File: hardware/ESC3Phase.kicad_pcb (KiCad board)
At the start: 2 copper layers, 0 parts

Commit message: PCB layout: board outline, mounting holes, footprint placement, copper pours, phase-output routing
- 100x115mm 2-layer board, 4x M3 mounting holes, design rules per PowerLab spec
- All 55 schematic components synced to board with real footprints
- Auto-placed via force-directed placement with locked connector/MCU anchors
- GND pour (both layers) + localized pours for VIN_RAW/+VBUS/+VBUS_EFUSE_OUT/+VBUS_PROT/+5V_LOGIC
- Routed the 3 critical phase-output traces (SHA/SHB/SHC, 2mm wide)
- Documented full PCB status in ARCHITECTURE.md: NOT yet fab-ready (732 DRC
  violations, 21 courtyard overlaps, ~50 signal nets still unrouted since
  Freerouting is unavailable in this environment)

Co-Authored-By: Claude Sonnet 5 <noreply@anthropic.com>
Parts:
- added C1: 100 nF, METUPowerLab_Capacitors_Ceramics_SurfaceMounts:0603_Medium, F.Cu at (70.1, 21.5)
- added C10: 100 nF, METUPowerLab_Capacitors_Ceramics_SurfaceMounts:0603_Medium, F.Cu at (46.5, 29.4)
- added C11: 100 nF, METUPowerLab_Capacitors_Ceramics_SurfaceMounts:0603_Medium, F.Cu at (52.2, 25.5)
- added C12: 1 nF, METUPowerLab_Capacitors_Ceramics_SurfaceMounts:0603_Medium, F.Cu at (68.9, 33.7)
- added C13: 10 nF, METUPowerLab_Capacitors_Ceramics_SurfaceMounts:0603_Medium, F.Cu at (73.1, 21.5)
- added C14: 1 nF, METUPowerLab_Capacitors_Ceramics_SurfaceMounts:0603_Medium, F.Cu at (66.8, 16.6)
- added C15: 22 pF, METUPowerLab_Capacitors_Ceramics_SurfaceMounts:0603_Medium, F.Cu at (77.8, 26.2)
- added C16: 4.7 µF, METUPowerLab_Capacitors_Ceramics_SurfaceMounts:0805_Medium, F.Cu at (71.5, 57.8)
- added C17: 100 nF, METUPowerLab_Capacitors_Ceramics_SurfaceMounts:0603_Medium, F.Cu at (68.7, 48.6)
- added C18: BOOT 100nF 16V+, METUPowerLab_Capacitors_Ceramics_SurfaceMounts:0603_Medium, F.Cu at (48.7, 26.1)
- added C19: 22 µF, METUPowerLab_Capacitors_Ceramics_SurfaceMounts:1210_Medium, F.Cu at (46.0, 25.7)
- added C2: 1 µF, METUPowerLab_Capacitors_Ceramics_SurfaceMounts:0603_Medium, F.Cu at (70.2, 16.4)
- added C20: 22 µF, METUPowerLab_Capacitors_Ceramics_SurfaceMounts:1210_Medium, F.Cu at (38.2, 41.9)
- added C21: 1 µF, METUPowerLab_Capacitors_Ceramics_SurfaceMounts:0603_Medium, F.Cu at (54.8, 24.9)
- added C22: 10 µF, METUPowerLab_Capacitors_Ceramics_SurfaceMounts:0805_Medium, F.Cu at (80.0, 24.3)
- added C23: CP flying cap, METUPowerLab_Capacitors_Ceramics_SurfaceMounts:0805_Medium, F.Cu at (50.8, 60.8)
- added C24: VCP decouple, METUPowerLab_Capacitors_Ceramics_SurfaceMounts:0603_Medium, F.Cu at (70.7, 62.4)
- added C25: VM hf decouple, METUPowerLab_Capacitors_Ceramics_SurfaceMounts:0603_Medium, F.Cu at (68.8, 45.9)
- added C26: VM bulk decouple, METUPowerLab_Capacitors_Ceramics_SurfaceMounts:2220, F.Cu at (57.3, 62.9)
- added C27: DVDD decouple, METUPowerLab_Capacitors_Ceramics_SurfaceMounts:0603_Medium, F.Cu at (42.7, 45.3)
- added C28: VREF decouple, METUPowerLab_Capacitors_Ceramics_SurfaceMounts:0603_Medium, F.Cu at (63.1, 49.2)
- added C29: Hot-loop bulk, METUPowerLab_Capacitors_Ceramics_SurfaceMounts:2220, F.Cu at (81.0, 47.1)
- added C3: 100 nF, METUPowerLab_Capacitors_Ceramics_SurfaceMounts:0603_Medium, F.Cu at (65.6, 31.0)
- added C30: Hot-loop bulk, METUPowerLab_Capacitors_Ceramics_SurfaceMounts:2220, F.Cu at (76.0, 57.3)
- added C31: DC bus bulk, METUPowerLab_Capacitors_AluminumPolymers_ThroughHoles:8.00x13.50mm, F.Cu at (96.0, 44.0)
- added C32: DC bus bulk, METUPowerLab_Capacitors_AluminumPolymers_ThroughHoles:8.00x13.50mm, F.Cu at (75.2, 45.5)
- added C33: INA240 decouple, METUPowerLab_Capacitors_Ceramics_SurfaceMounts:0603_Medium, F.Cu at (67.2, 25.5)
- added C34: CAN txcvr decouple, METUPowerLab_Capacitors_Ceramics_SurfaceMounts:0603_Medium, F.Cu at (66.1, 20.1)
- added D1: SMBJ48CA-13-F, METUPowerLab_Diodes_TVSDiodes:DO-214AA, F.Cu at (33.4, 26.6)
- added D2: CANH ESD, METUPowerLab_Diodes_TVSDiodes:0603_Small, F.Cu at (91.1, 44.8)
- added D3: CANL ESD, METUPowerLab_Diodes_TVSDiodes:0603_Small, F.Cu at (88.9, 44.9)
- added J1: UART_HDR, METUPowerLab_Connectors_SignalConnectors:2147210040, F.Cu at (74.0, 12.0)
- added J2: EXP_HDR, METUPowerLab_Connectors_SignalConnectors:384471-E, F.Cu at (82.5, 25.0)
- added J3: VIN+, METUPowerLab_Connectors_ScrewTerminals:7770, F.Cu at (20.0, 18.0)
- added J4: GND, METUPowerLab_Connectors_ScrewTerminals:7770, F.Cu at (30.0, 15.0)
- added J5: PHASE_A, METUPowerLab_Connectors_ScrewTerminals:7770, F.Cu at (18.0, 95.0)
- added J6: PHASE_B, METUPowerLab_Connectors_ScrewTerminals:7770, F.Cu at (45.0, 95.0)
- added J7: PHASE_C, METUPowerLab_Connectors_ScrewTerminals:7770, F.Cu at (72.0, 95.0)
- added J8: CAN_BUS, METUPowerLab_Connectors_SignalConnectors:384471-E, F.Cu at (82.5, 70.0)
- added L1: 6.8µH, METUPowerLab_Inductors_SurfaceMounts:6x6mm, F.Cu at (37.6, 37.0)
- added MH1: MountingHole_3.2mm, MountingHole:MountingHole_3.2mm, F.Cu at (8.00, 8.00)
- added MH2: MountingHole_3.2mm, MountingHole:MountingHole_3.2mm, F.Cu at (92.0, 8.00)
- added MH3: MountingHole_3.2mm, MountingHole:MountingHole_3.2mm, F.Cu at (8.00, 107.0)
- added MH4: MountingHole_3.2mm, MountingHole:MountingHole_3.2mm, F.Cu at (92.0, 107.0)
- added Q1: RevPol, METUPowerLab_Transistors_MOSFETs:8-PowerTDFN(5x6mm), F.Cu at (53.1, 9.98)
- added Q2: Phase A high-side, METUPowerLab_Transistors_MOSFETs:8-PowerTDFN(5x6mm), F.Cu at (54.3, 71.9)
- added Q3: Phase A low-side, METUPowerLab_Transistors_MOSFETs:8-PowerTDFN(5x6mm), F.Cu at (47.9, 69.6)
- added Q4: Phase B high-side, METUPowerLab_Transistors_MOSFETs:8-PowerTDFN(5x6mm), F.Cu at (68.7, 80.4)
- added Q5: Phase B low-side, METUPowerLab_Transistors_MOSFETs:8-PowerTDFN(5x6mm), F.Cu at (39.5, 58.5)
- added Q6: Phase C high-side, METUPowerLab_Transistors_MOSFETs:8-PowerTDFN(5x6mm), F.Cu at (69.0, 70.9)
- added Q7: Phase C low-side, METUPowerLab_Transistors_MOSFETs:8-PowerTDFN(5x6mm), F.Cu at (61.3, 72.0)
- added R1: 10 kOhm, METUPowerLab_Resistors_ChipResistors:0603_Medium, F.Cu at (78.3, 21.0)
- added R10: 10 kOhm, METUPowerLab_Resistors_ChipResistors:0603_Medium, F.Cu at (77.7, 23.6)
- added R11: 10 kOhm, METUPowerLab_Resistors_ChipResistors:0603_Medium, F.Cu at (70.1, 19.0)
- added R12: RT 22.1k (~1.1MHz), METUPowerLab_Resistors_ChipResistors:0603_Medium, F.Cu at (61.5, 56.3)
- added R13: 88.7 kOhm, METUPowerLab_Resistors_ChipResistors:0603_Medium, F.Cu at (50.9, 29.7)
- added R14: 22.1 kOhm, METUPowerLab_Resistors_ChipResistors:0603_Medium, F.Cu at (68.9, 30.3)
- added R15: 100 kOhm, METUPowerLab_Resistors_ChipResistors:0603_Medium, F.Cu at (50.7, 20.9)
- added R16: INHA pulldown, METUPowerLab_Resistors_ChipResistors:0603_Medium, F.Cu at (61.5, 51.1)
- added R17: INLA pulldown, METUPowerLab_Resistors_ChipResistors:0603_Medium, F.Cu at (61.5, 53.7)
- added R18: INHB pulldown, METUPowerLab_Resistors_ChipResistors:0603_Medium, F.Cu at (65.7, 48.1)
- added R19: INLB pulldown, METUPowerLab_Resistors_ChipResistors:0603_Medium, F.Cu at (65.8, 33.1)
- added R2: 10 kOhm, METUPowerLab_Resistors_ChipResistors:0603_Medium, F.Cu at (64.2, 25.6)
- added R20: INHC pulldown, METUPowerLab_Resistors_ChipResistors:0603_Medium, F.Cu at (65.8, 45.5)
- added R21: INLC pulldown, METUPowerLab_Resistors_ChipResistors:0603_Medium, F.Cu at (60.0, 39.7)
- added R22: ENABLE pulldown, METUPowerLab_Resistors_ChipResistors:0603_Medium, F.Cu at (61.4, 41.9)
- added R23: SDO pullup, METUPowerLab_Resistors_ChipResistors:0603_Medium, F.Cu at (73.2, 26.0)
- added R3: 10 kOhm, METUPowerLab_Resistors_ChipResistors:0603_Medium, F.Cu at (66.2, 22.7)
- added R4: 120 Ohm, METUPowerLab_Resistors_ChipResistors:0603_Medium, F.Cu at (48.7, 23.5)
- added R5: 866 kOhm, METUPowerLab_Resistors_ChipResistors:0603_Medium, F.Cu at (52.6, 18.5)
- added R6: 118 kOhm, METUPowerLab_Resistors_ChipResistors:0603_Medium, F.Cu at (63.1, 45.7)
- added R7: 1.2 kOhm, METUPowerLab_Resistors_ChipResistors:0603_Medium, F.Cu at (70.2, 26.7)
- added R8: 3 kOhm, METUPowerLab_Resistors_ChipResistors:0603_Medium, F.Cu at (70.2, 24.1)
- added R9: 10 kOhm, METUPowerLab_Resistors_ChipResistors:0603_Medium, F.Cu at (68.9, 13.8)
- added RS1: Phase A shunt, METUPowerLab_Resistors_ShuntResistors:2010, F.Cu at (47.3, 39.7)
- added RS2: Phase B shunt, METUPowerLab_Resistors_ShuntResistors:2010, F.Cu at (39.9, 47.7)
- added RS3: Phase C shunt, METUPowerLab_Resistors_ShuntResistors:2010, F.Cu at (50.5, 55.7)
- added RS4: DC bus shunt, METUPowerLab_Resistors_ShuntResistors:2010, F.Cu at (68.9, 54.5)
- added SW1: RESET, METUPowerLab_Switches_TactileSwitches:TL6330AF200Q, F.Cu at (74.2, 32.9)
- added SW2: BOOT, METUPowerLab_Switches_TactileSwitches:TL6330AF200Q, F.Cu at (75.8, 12.2)
- added U1: ESP32-WROOM-32E, METUPowerLab_Microcontrollers_ESP32:ESP32-WROOM-32E, F.Cu at (55.0, 25.0)
- added U10: SN65HVD230DR, METUPowerLab_Interfaces_CANBusBridges:8-SOIC, F.Cu at (81.1, 34.6)
- added U2: LM5050-1, METUPowerLab_CircuitProtections_IdealDiodes:SOT-23-6, F.Cu at (40.0, 26.4)
- added U3: PTPS16890VMAR, METUPowerLab_CircuitProtections_eFuses:23-LQFN-CLIP_(VMA), F.Cu at (57.2, 26.2)
- added U4: LMR38020FSDDAR, METUPowerLab_Regulators_BuckConverters:8-SOICPower, F.Cu at (46.9, 50.2)
- added U5: NCP1117ST33T3G, METUPowerLab_Regulators_LDOs:SOT-223, F.Cu at (57.3, 16.7)
- added U6: DRV8323RSRGZT, METUPowerLab_MotorDrivers_BLDC:48-VQFN, F.Cu at (53.1, 49.0)
- added U8: TMP235A4DCKR, METUPowerLab_Sensors_Temperature:SC-70-5, F.Cu at (73.5, 19.4)
- added U9: INA240A4DR, METUPowerLab_Amplifiers_CurrentSenses:8-SOIC, F.Cu at (69.9, 42.6)
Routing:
- net SHB: track 0.00 -> 33.3 mm
- net SHA: track 0.00 -> 31.3 mm
- net SHC: track 0.00 -> 21.8 mm
- added copper zone on F.Cu, net +5V_LOGIC
- added copper zone on F.Cu, net +VBUS
- added copper zone on F.Cu, net +VBUS_EFUSE_OUT
- added copper zone on F.Cu, net +VBUS_PROT
- added copper zone on B.Cu, net GND
- added copper zone on F.Cu, net GND
- added copper zone on F.Cu, net VIN_RAW
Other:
- board outline added: 100 x 115 mm

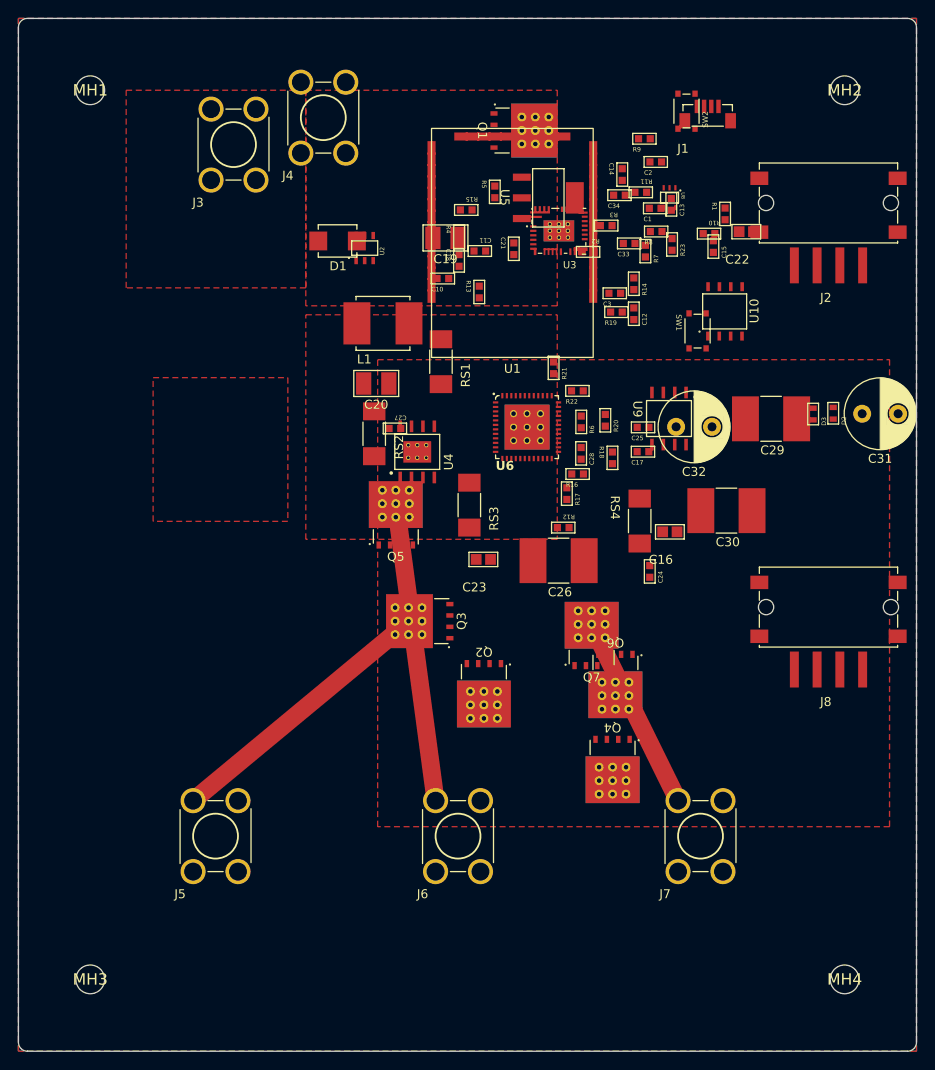
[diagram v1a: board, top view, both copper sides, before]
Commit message: PCB: fix all real courtyard overlaps, route every net, add +3V3_MCU pour
- Resolved all 44 real footprint/pad collisions via targeted placement
  fixes (verified pad-by-pad); 5 residual flags are a vendor-footprint
  bounding-box artifact on the PowerTDFN MOSFETs, not real collisions
- Hid the 4 mounting holes' oversized reference/value silkscreen text
  that was hanging off the board edge
- Added a +3V3_MCU copper pour (18-pad fanout, same pattern as the
  other power rails)
- Routed every remaining net on the board: PWM gate-drive x6 + pulldowns,
  ENABLE/nFAULT/EN, SPI, CAN, UART, ADC sense lines, buck converter
  network, all 9 eFuse config lines, charge pump, VREF/DVDD decouple,
  BOOT strap, REVPOL_GATE, expansion header. Zero unconnected nets.
- SNA/SNB/SNC (shunt Kelvin sense) intentionally left unrouted: the
  vendor shunt footprint only exposes 2 physical pads for 4 schematic
  pins, so there is no copper to route the sense lines to (documented
  in ARCHITECTURE.md as a vendor library limitation, not an oversight)
- Traces were routed as direct point-to-point segments (no autorouter
  available in this environment), so they cut across existing pours/
  traces without respecting clearance — DRC violations rose from 732 to
  826. Net-list completeness is done; DRC-clean routing is not.

Co-Authored-By: Claude Sonnet 5 <noreply@anthropic.com>
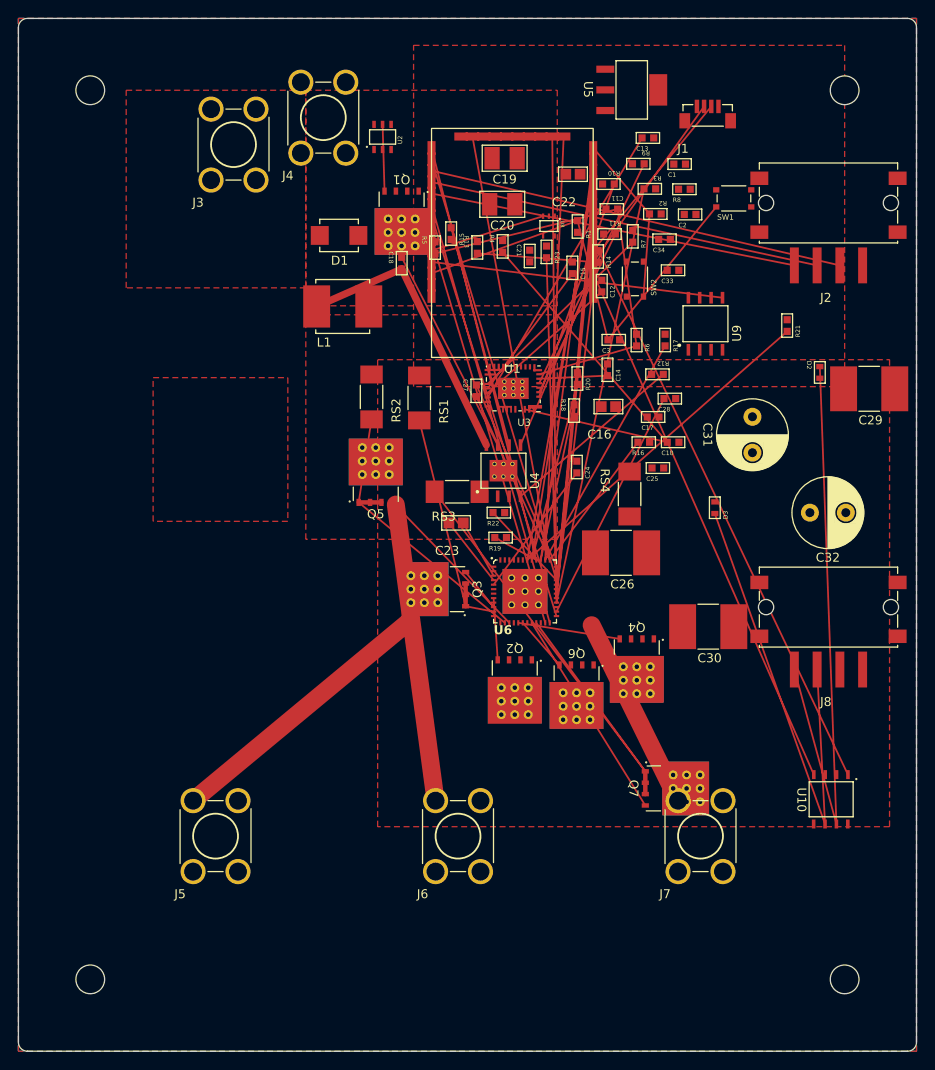
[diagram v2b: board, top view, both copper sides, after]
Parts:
- moved U10 50.9 mm to (88.0, 85.0), turned to -90 degrees
- moved C10 31.5 mm to (72.1, 47.6)
- moved R19 28.2 mm to (52.9, 58.2)
- moved R21 26.4 mm to (86.0, 35.0)
- moved C20 24.4 mm to (52.3, 21.9)
- moved C14 23.4 mm to (66.0, 39.9), turned to 90 degrees
- moved C22 20.3 mm to (60.7, 18.0)
- moved R17 20.3 mm to (72.4, 36.6)
- moved R12 20.0 mm to (72.0, 39.2)
- moved SW2 19.6 mm to (70.0, 30.9)
- moved U6 18.3 mm to (52.9, 67.3)
- moved U3 18.3 mm to (52.1, 43.7)
- moved C32 17.7 mm to (90.1, 55.0)
- moved R22 16.1 mm to (52.7, 55.4)
- moved R1 15.9 mm to (62.7, 24.0), turned to 90 degrees
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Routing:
- net nFAULT: track 0.00 -> 99.0 mm
- net INHA: track 0.00 -> 84.3 mm
- net INLC: track 0.00 -> 81.2 mm
- net SDO: track 0.00 -> 80.6 mm
- net INLA: track 0.00 -> 74.5 mm
- net CANH: track 0.00 -> 68.8 mm
- net CAN_TX: track 0.00 -> 66.0 mm
- net INHC: track 0.00 -> 64.1 mm
- net INHB: track 0.00 -> 62.7 mm
- net SPC: track 0.00 -> 62.0 mm
- net CAN_RX: track 0.00 -> 61.0 mm
- net ENABLE: track 0.00 -> 59.2 mm
- net CANL: track 0.00 -> 53.9 mm
- net INLB: track 0.00 -> 52.6 mm
- net EN: track 0.00 -> 50.1 mm
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- added copper zone on F.Cu, net +3V3_MCU
